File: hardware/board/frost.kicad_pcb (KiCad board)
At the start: 2 copper layers, 90 x 55 mm, 12 parts, among them U1 RK3568, U2 K4UCE3Q4AB-MGCL, U3 KLMBG2JETD-B041_C5821038, U4 RK809-5, U5 AP6256, X1 24 MHz

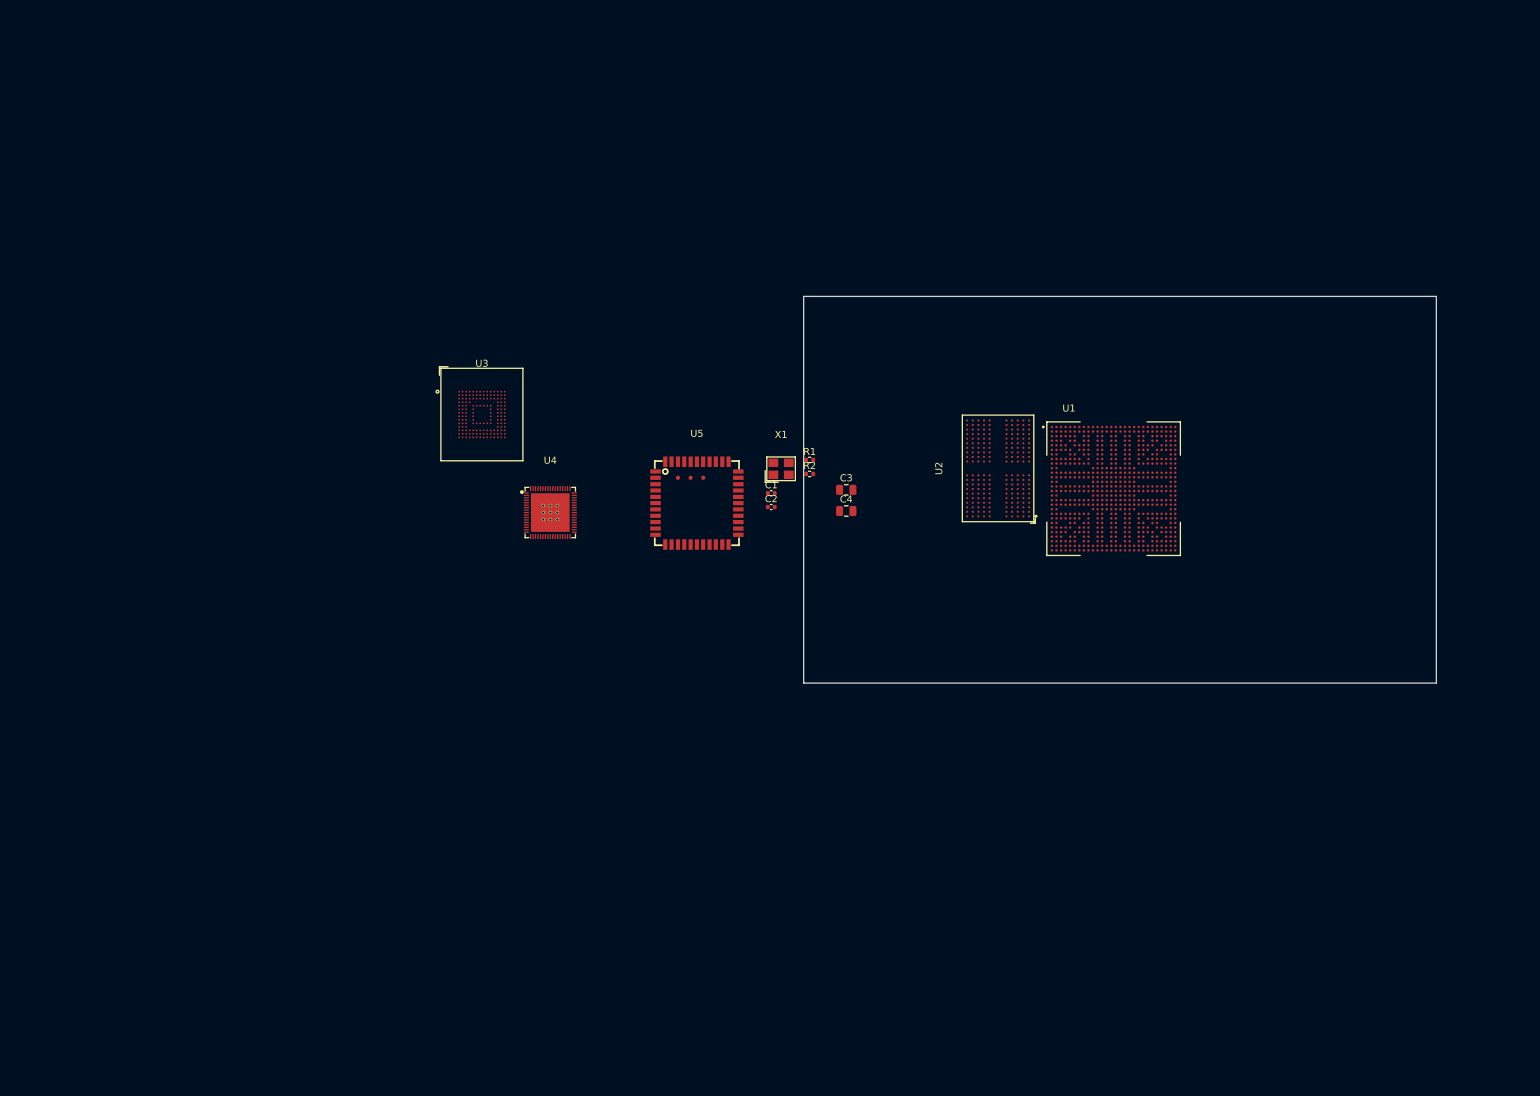
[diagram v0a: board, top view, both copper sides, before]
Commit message: MIPI IS FAKE
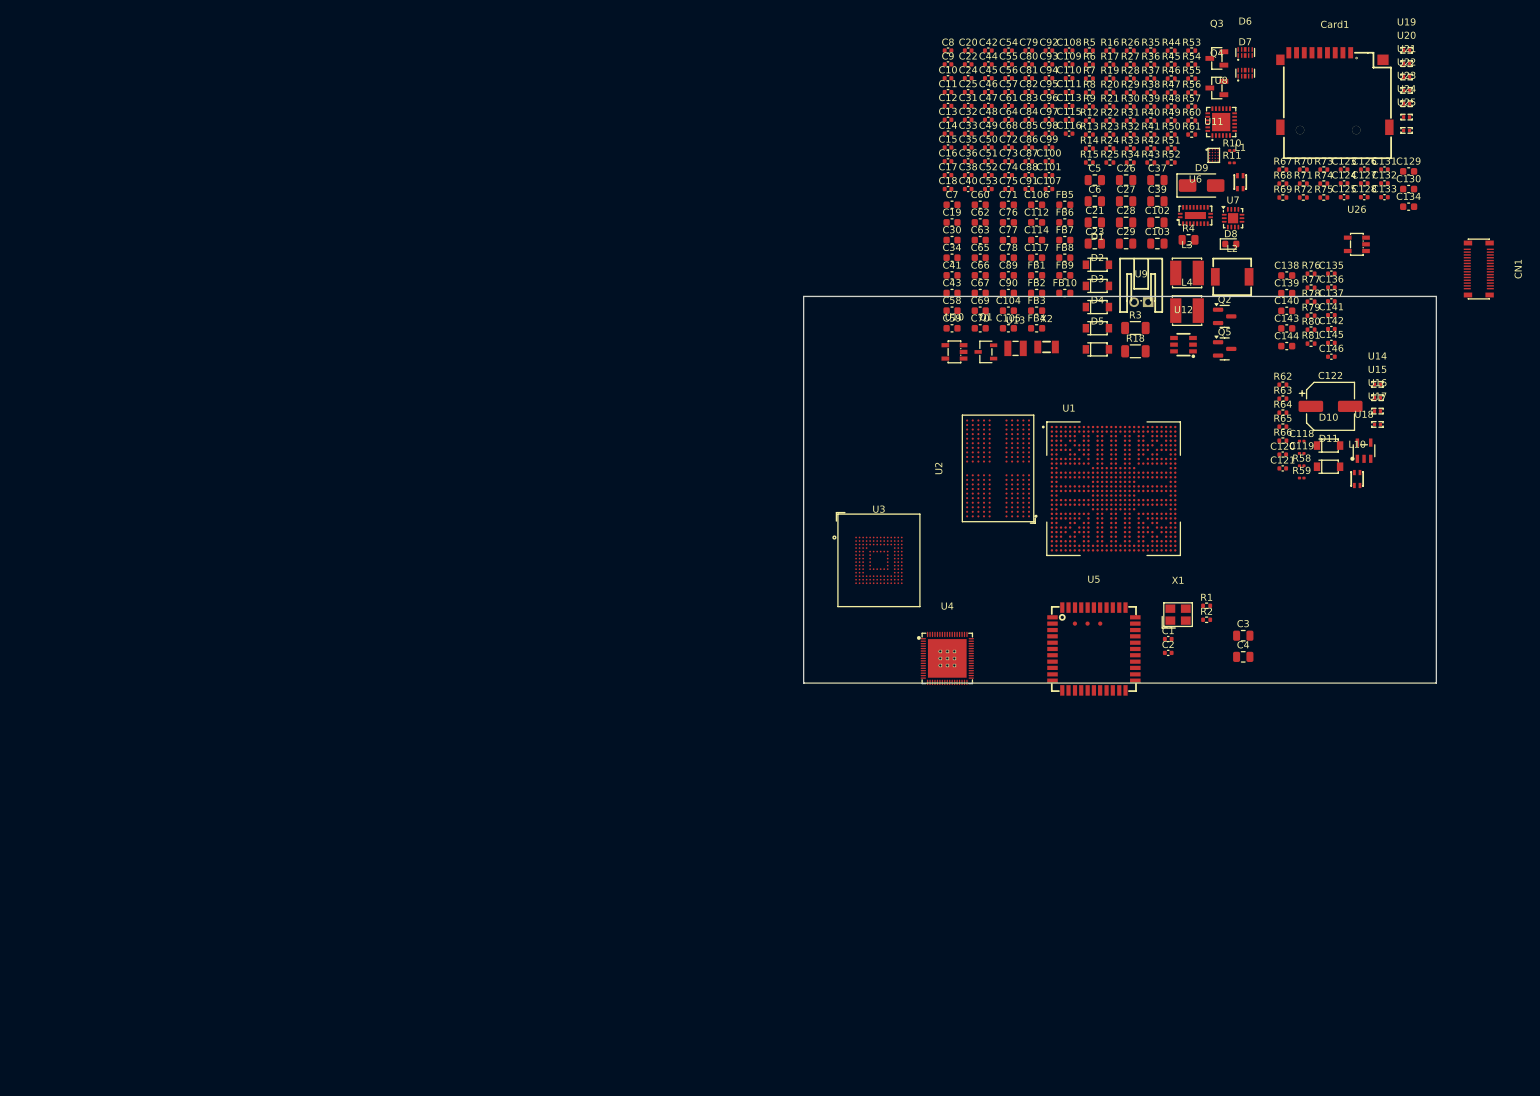
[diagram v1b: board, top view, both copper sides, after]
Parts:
- added C10: 100nF X5R 10V, Capacitor_SMD:C_0402_1005Metric, F.Cu at (149.6, 27.6)
- added C100: 680pF C0G 50V, Capacitor_SMD:C_0402_1005Metric, F.Cu at (163.9, 39.5)
- added C101: 1uF X5R 6.3V, Capacitor_SMD:C_0402_1005Metric, F.Cu at (163.9, 41.4)
- added C102: 22uF X5R 10V, Capacitor_SMD:C_0805_2012Metric, F.Cu at (179.4, 48.1)
- added C103: 22uF X5R 10V, Capacitor_SMD:C_0805_2012Metric, F.Cu at (179.4, 51.2)
- added C104: 22uF X5R 6.3V, Capacitor_SMD:C_0603_1608Metric, F.Cu at (158.2, 60.7)
- added C105: 22uF X5R 6.3V, Capacitor_SMD:C_0603_1608Metric, F.Cu at (158.2, 63.2)
- added C106: 22uF X5R 6.3V, Capacitor_SMD:C_0603_1608Metric, F.Cu at (162.2, 45.6)
- added C107: 1uF X5R 6.3V, Capacitor_SMD:C_0402_1005Metric, F.Cu at (163.9, 43.4)
- added C108: 1uF X5R 6.3V, Capacitor_SMD:C_0402_1005Metric, F.Cu at (166.8, 23.7)
- added C109: 1uF X5R 6.3V, Capacitor_SMD:C_0402_1005Metric, F.Cu at (166.8, 25.7)
- added C11: 100nF X5R 10V, Capacitor_SMD:C_0402_1005Metric, F.Cu at (149.6, 29.6)
- added C110: 1uF X5R 6.3V, Capacitor_SMD:C_0402_1005Metric, F.Cu at (166.8, 27.6)
- added C111: 1uF X5R 6.3V, Capacitor_SMD:C_0402_1005Metric, F.Cu at (166.8, 29.6)
- added C112: 10uF X5R 10V, Capacitor_SMD:C_0603_1608Metric, F.Cu at (162.2, 48.1)
- added C113: 100nF X5R 10V, Capacitor_SMD:C_0402_1005Metric, F.Cu at (166.8, 31.6)
- added C114: 10uF X5R 10V, Capacitor_SMD:C_0603_1608Metric, F.Cu at (162.2, 50.7)
- added C115: 1uF X5R 6.3V, Capacitor_SMD:C_0402_1005Metric, F.Cu at (166.8, 33.5)
- added C116: 1uF X5R 6.3V, Capacitor_SMD:C_0402_1005Metric, F.Cu at (166.8, 35.5)
- added C117: 4.7uF X5R 6.3V, Capacitor_SMD:C_0603_1608Metric, F.Cu at (162.2, 53.2)
- added C118: 100nF X5R 10V, Capacitor_SMD:C_0201_0603Metric, F.Cu at (199.9, 79.3)
- added C119: 100nF X5R 10V, Capacitor_SMD:C_0201_0603Metric, F.Cu at (199.9, 81.0)
- added C12: 100nF X5R 10V, Capacitor_SMD:C_0402_1005Metric, F.Cu at (149.6, 31.6)
- added C120: 1uF X5R 10V, Capacitor_SMD:C_0402_1005Metric, F.Cu at (197.2, 81.2)
- added C121: 100nF X5R 10V, Capacitor_SMD:C_0402_1005Metric, F.Cu at (197.2, 83.1)
- added C122: 120uF SVPF 20V, Capacitor_SMD:CP_Elec_6.3x5.9, F.Cu at (204.0, 74.3)
- added C123: 2.2uF X5R 10V, Capacitor_SMD:C_0402_1005Metric, F.Cu at (205.9, 40.6)
- added C124: 100nF X5R 10V, Capacitor_SMD:C_0402_1005Metric, F.Cu at (205.9, 42.6)
- added C125: 100nF X5R 10V, Capacitor_SMD:C_0402_1005Metric, F.Cu at (205.9, 44.6)
- added C126: 100nF X5R 10V, Capacitor_SMD:C_0402_1005Metric, F.Cu at (208.8, 40.6)
- added C127: 100nF X5R 10V, Capacitor_SMD:C_0402_1005Metric, F.Cu at (208.8, 42.6)
- added C128: 100nF X5R 10V, Capacitor_SMD:C_0402_1005Metric, F.Cu at (208.8, 44.6)
- added C129: 4.7uF X5R 6.3V, Capacitor_SMD:C_0603_1608Metric, F.Cu at (215.1, 40.9)
- added C13: 100nF X5R 10V, Capacitor_SMD:C_0402_1005Metric, F.Cu at (149.6, 33.5)
- added C130: 4.7uF X5R 6.3V, Capacitor_SMD:C_0603_1608Metric, F.Cu at (215.1, 43.4)
- added C131: 100nF X5R 10V, Capacitor_SMD:C_0402_1005Metric, F.Cu at (211.7, 40.6)
- added C132: 100nF X5R 10V, Capacitor_SMD:C_0402_1005Metric, F.Cu at (211.7, 42.6)
- added C133: 100nF X5R 10V, Capacitor_SMD:C_0402_1005Metric, F.Cu at (211.7, 44.6)
- added C134: 10uF X5R 10V, Capacitor_SMD:C_0603_1608Metric, F.Cu at (215.1, 45.9)
- added C135: 1uF X5R 6.3V, Capacitor_SMD:C_0402_1005Metric, F.Cu at (204.1, 55.4)
- added C136: 100nF X5R 10V, Capacitor_SMD:C_0402_1005Metric, F.Cu at (204.1, 57.4)
- added C137: 22pF C0G 50V, Capacitor_SMD:C_0402_1005Metric, F.Cu at (204.1, 59.4)
- added C138: 10uF X5R 10V, Capacitor_SMD:C_0603_1608Metric, F.Cu at (197.8, 55.7)
- added C139: 4.7uF X5R 6.3V, Capacitor_SMD:C_0603_1608Metric, F.Cu at (197.8, 58.2)
- added C14: 100nF X5R 10V, Capacitor_SMD:C_0402_1005Metric, F.Cu at (149.6, 35.5)
- added C140: 4.7uF X5R 6.3V, Capacitor_SMD:C_0603_1608Metric, F.Cu at (197.8, 60.7)
- added C141: 100nF X5R 10V, Capacitor_SMD:C_0402_1005Metric, F.Cu at (204.1, 61.3)
- added C142: 100nF X5R 10V, Capacitor_SMD:C_0402_1005Metric, F.Cu at (204.1, 63.3)
- added C143: 10uF X5R 10V, Capacitor_SMD:C_0603_1608Metric, F.Cu at (197.8, 63.2)
- added C144: 10uF X5R 10V, Capacitor_SMD:C_0603_1608Metric, F.Cu at (197.8, 65.7)
- added C145: 100nF X5R 10V, Capacitor_SMD:C_0402_1005Metric, F.Cu at (204.1, 65.3)
- added C146: 100nF X5R 10V, Capacitor_SMD:C_0402_1005Metric, F.Cu at (204.1, 67.2)
- added C15: 100nF X5R 10V, Capacitor_SMD:C_0402_1005Metric, F.Cu at (149.6, 37.5)
- added C16: 220pF C0G 25V, Capacitor_SMD:C_0402_1005Metric, F.Cu at (149.6, 39.5)
- added C17: 220pF C0G 25V, Capacitor_SMD:C_0402_1005Metric, F.Cu at (149.6, 41.4)
- added C18: 1uF X5R 10V, Capacitor_SMD:C_0402_1005Metric, F.Cu at (149.6, 43.4)
- added C19: 10uF X5R 10V, Capacitor_SMD:C_0603_1608Metric, F.Cu at (150.2, 48.1)
- added C20: 100nF X5R 10V, Capacitor_SMD:C_0402_1005Metric, F.Cu at (152.5, 23.7)
- added C21: 10uF X5R 25V, Capacitor_SMD:C_0805_2012Metric, F.Cu at (170.5, 48.1)
- added C22: 100pF C0G 50V, Capacitor_SMD:C_0402_1005Metric, F.Cu at (152.5, 25.7)
- added C23: 10uF X5R 25V, Capacitor_SMD:C_0805_2012Metric, F.Cu at (170.5, 51.2)
- added C24: 4.7uF X5R 10V, Capacitor_SMD:C_0402_1005Metric, F.Cu at (152.5, 27.6)
- added C25: 47nF X5R 25V, Capacitor_SMD:C_0402_1005Metric, F.Cu at (152.5, 29.6)
- added C26: 10uF X5R 10V, Capacitor_SMD:C_0805_2012Metric, F.Cu at (174.9, 42.1)
- added C27: 10uF X5R 10V, Capacitor_SMD:C_0805_2012Metric, F.Cu at (174.9, 45.1)
- added C28: 10uF X5R 10V, Capacitor_SMD:C_0805_2012Metric, F.Cu at (174.9, 48.1)
- added C29: 10uF X5R 10V, Capacitor_SMD:C_0805_2012Metric, F.Cu at (174.9, 51.2)
- added C30: 10uF X5R 10V, Capacitor_SMD:C_0603_1608Metric, F.Cu at (150.2, 50.7)
- added C31: 100nF X5R 10V, Capacitor_SMD:C_0402_1005Metric, F.Cu at (152.5, 31.6)
- added C32: 100nF X5R 10V, Capacitor_SMD:C_0402_1005Metric, F.Cu at (152.5, 33.5)
- added C33: 22pF C0G 50V, Capacitor_SMD:C_0402_1005Metric, F.Cu at (152.5, 35.5)
- added C34: 22uF X5R 6.3V, Capacitor_SMD:C_0603_1608Metric, F.Cu at (150.2, 53.2)
- added C35: 100nF X5R 10V, Capacitor_SMD:C_0402_1005Metric, F.Cu at (152.5, 37.5)
- added C36: 100nF X5R 16V, Capacitor_SMD:C_0402_1005Metric, F.Cu at (152.5, 39.5)
- added C37: 10uF X5R 10V, Capacitor_SMD:C_0805_2012Metric, F.Cu at (179.4, 42.1)
- added C38: 22pF C0G 50V, Capacitor_SMD:C_0402_1005Metric, F.Cu at (152.5, 41.4)
- added C39: 22uF X5R 10V, Capacitor_SMD:C_0805_2012Metric, F.Cu at (179.4, 45.1)
- added C40: 100nF X5R 10V, Capacitor_SMD:C_0402_1005Metric, F.Cu at (152.5, 43.4)
- added C41: 10uF X5R 10V, Capacitor_SMD:C_0603_1608Metric, F.Cu at (150.2, 55.7)
- added C42: 100nF X5R 10V, Capacitor_SMD:C_0402_1005Metric, F.Cu at (155.3, 23.7)
- added C43: 10uF X5R 10V, Capacitor_SMD:C_0603_1608Metric, F.Cu at (150.2, 58.2)
- added C44: 4.7uF X5R 6.3V, Capacitor_SMD:C_0402_1005Metric, F.Cu at (155.3, 25.7)
- added C45: 1uF X5R 6.3V, Capacitor_SMD:C_0402_1005Metric, F.Cu at (155.3, 27.6)
- added C46: 1uF X5R 6.3V, Capacitor_SMD:C_0402_1005Metric, F.Cu at (155.3, 29.6)
- added C47: 1uF X5R 6.3V, Capacitor_SMD:C_0402_1005Metric, F.Cu at (155.3, 31.6)
- added C48: 1uF X5R 6.3V, Capacitor_SMD:C_0402_1005Metric, F.Cu at (155.3, 33.5)
- added C49: 1uF X5R 6.3V, Capacitor_SMD:C_0402_1005Metric, F.Cu at (155.3, 35.5)
- added C5: 10uF X5R 25V, Capacitor_SMD:C_0805_2012Metric, F.Cu at (170.5, 42.1)
- added C50: 1uF X5R 10V, Capacitor_SMD:C_0402_1005Metric, F.Cu at (155.3, 37.5)
- added C51: 20pF C0G 50V, Capacitor_SMD:C_0402_1005Metric, F.Cu at (155.3, 39.5)
- added C52: 20pF C0G 50V, Capacitor_SMD:C_0402_1005Metric, F.Cu at (155.3, 41.4)
- added C53: 100nF X5R 10V, Capacitor_SMD:C_0402_1005Metric, F.Cu at (155.3, 43.4)
- added C54: 100nF X5R 10V, Capacitor_SMD:C_0402_1005Metric, F.Cu at (158.2, 23.7)
- added C55: 100nF X5R 16V, Capacitor_SMD:C_0402_1005Metric, F.Cu at (158.2, 25.7)
- added C56: 100nF X5R 16V, Capacitor_SMD:C_0402_1005Metric, F.Cu at (158.2, 27.6)
- added C57: 1uF X5R 10V, Capacitor_SMD:C_0402_1005Metric, F.Cu at (158.2, 29.6)
- added C58: 22uF X5R 6.3V, Capacitor_SMD:C_0603_1608Metric, F.Cu at (150.2, 60.7)
- added C59: 22uF X5R 6.3V, Capacitor_SMD:C_0603_1608Metric, F.Cu at (150.2, 63.2)
- added C6: 10uF X5R 25V, Capacitor_SMD:C_0805_2012Metric, F.Cu at (170.5, 45.1)
- added C60: 22uF X5R 6.3V, Capacitor_SMD:C_0603_1608Metric, F.Cu at (154.2, 45.6)
- added C61: 100nF X5R 10V, Capacitor_SMD:C_0402_1005Metric, F.Cu at (158.2, 31.6)
- added C62: 22uF X5R 6.3V, Capacitor_SMD:C_0603_1608Metric, F.Cu at (154.2, 48.1)
- added C63: 22uF X5R 6.3V, Capacitor_SMD:C_0603_1608Metric, F.Cu at (154.2, 50.7)
- added C64: 100nF X5R 10V, Capacitor_SMD:C_0402_1005Metric, F.Cu at (158.2, 33.5)
- added C65: 10uF X5R 10V, Capacitor_SMD:C_0603_1608Metric, F.Cu at (154.2, 53.2)
- added C66: 22uF X5R 6.3V, Capacitor_SMD:C_0603_1608Metric, F.Cu at (154.2, 55.7)
- added C67: 22uF X5R 6.3V, Capacitor_SMD:C_0603_1608Metric, F.Cu at (154.2, 58.2)
- added C68: 100nF X5R 10V, Capacitor_SMD:C_0402_1005Metric, F.Cu at (158.2, 35.5)
- added C69: 10uF X5R 10V, Capacitor_SMD:C_0603_1608Metric, F.Cu at (154.2, 60.7)
- added C7: 10uF X5R 10V, Capacitor_SMD:C_0603_1608Metric, F.Cu at (150.2, 45.6)
- added C70: 22uF X5R 6.3V, Capacitor_SMD:C_0603_1608Metric, F.Cu at (154.2, 63.2)
- added C71: 10uF X5R 10V, Capacitor_SMD:C_0603_1608Metric, F.Cu at (158.2, 45.6)
- added C72: 1uF X5R 6.3V, Capacitor_SMD:C_0402_1005Metric, F.Cu at (158.2, 37.5)
- added C73: 1uF X5R 6.3V, Capacitor_SMD:C_0402_1005Metric, F.Cu at (158.2, 39.5)
- added C74: 1uF X5R 10V, Capacitor_SMD:C_0402_1005Metric, F.Cu at (158.2, 41.4)
- added C75: 1uF X5R 6.3V, Capacitor_SMD:C_0402_1005Metric, F.Cu at (158.2, 43.4)
- added C76: 10uF X5R 10V, Capacitor_SMD:C_0603_1608Metric, F.Cu at (158.2, 48.1)
- added C77: 22uF X5R 6.3V, Capacitor_SMD:C_0603_1608Metric, F.Cu at (158.2, 50.7)
- added C78: 22uF X5R 6.3V, Capacitor_SMD:C_0603_1608Metric, F.Cu at (158.2, 53.2)
- added C79: 1uF X5R 6.3V, Capacitor_SMD:C_0402_1005Metric, F.Cu at (161.1, 23.7)
- added C8: 100nF X5R 10V, Capacitor_SMD:C_0402_1005Metric, F.Cu at (149.6, 23.7)
- added C80: 100nF X5R 10V, Capacitor_SMD:C_0402_1005Metric, F.Cu at (161.1, 25.7)
- added C81: 1uF X5R 6.3V, Capacitor_SMD:C_0402_1005Metric, F.Cu at (161.1, 27.6)
- added C82: 1uF X5R 6.3V, Capacitor_SMD:C_0402_1005Metric, F.Cu at (161.1, 29.6)
- added C83: 1uF X5R 10V, Capacitor_SMD:C_0402_1005Metric, F.Cu at (161.1, 31.6)
- added C84: 1uF X5R 10V, Capacitor_SMD:C_0402_1005Metric, F.Cu at (161.1, 33.5)
- added C85: 1uF X5R 10V, Capacitor_SMD:C_0402_1005Metric, F.Cu at (161.1, 35.5)
- added C86: 4.7uF X5R 6.3V, Capacitor_SMD:C_0402_1005Metric, F.Cu at (161.1, 37.5)
- added C87: 1uF X5R 6.3V, Capacitor_SMD:C_0402_1005Metric, F.Cu at (161.1, 39.5)
- added C88: 1uF X5R 6.3V, Capacitor_SMD:C_0402_1005Metric, F.Cu at (161.1, 41.4)
- added C89: 10uF X5R 10V, Capacitor_SMD:C_0603_1608Metric, F.Cu at (158.2, 55.7)
- added C9: 100nF X5R 10V, Capacitor_SMD:C_0402_1005Metric, F.Cu at (149.6, 25.7)
- added C90: 4.7uF X5R 10V, Capacitor_SMD:C_0603_1608Metric, F.Cu at (158.2, 58.2)
- added C91: 1uF X5R 6.3V, Capacitor_SMD:C_0402_1005Metric, F.Cu at (161.1, 43.4)
- added C92: 2.2uF X5R 10V, Capacitor_SMD:C_0402_1005Metric, F.Cu at (163.9, 23.7)
- added C93: 1uF X5R 6.3V, Capacitor_SMD:C_0402_1005Metric, F.Cu at (163.9, 25.7)
- added C94: 1uF X5R 6.3V, Capacitor_SMD:C_0402_1005Metric, F.Cu at (163.9, 27.6)
- added C95: 27pF C0G 50V, Capacitor_SMD:C_0402_1005Metric, F.Cu at (163.9, 29.6)
- added C96: 27pF C0G 50V, Capacitor_SMD:C_0402_1005Metric, F.Cu at (163.9, 31.6)
- added C97: 100nF X5R 10V, Capacitor_SMD:C_0402_1005Metric, F.Cu at (163.9, 33.5)
- added C98: 100nF X5R 10V, Capacitor_SMD:C_0402_1005Metric, F.Cu at (163.9, 35.5)
- added C99: 680pF C0G 50V, Capacitor_SMD:C_0402_1005Metric, F.Cu at (163.9, 37.5)
- added CN1: AXT530124_C2924271, lcsc:CONN-SMD_30P-P0.40_AXT530124, F.Cu at (225.1, 54.8)
- added Card1: TF PUSH, lcsc:TF-SMD_TF-PUSH, F.Cu at (204.6, 29.3)
- added D1: BZT52C5V1_C173407, lcsc:SOD-123_L2.7-W1.6-LS3.7-RD, F.Cu at (170.8, 54.2)
- added D10: BZT52C5V1_C173407, lcsc:SOD-123_L2.7-W1.6-LS3.7-RD, F.Cu at (203.7, 79.9)
- added D11: BZT52C5V1_C173407, lcsc:SOD-123_L2.7-W1.6-LS3.7-RD, F.Cu at (203.7, 82.9)
- added D2: BZT52C5V1_C173407, lcsc:SOD-123_L2.7-W1.6-LS3.7-RD, F.Cu at (170.8, 57.2)
- added D3: BZT52C5V1_C173407, lcsc:SOD-123_L2.7-W1.6-LS3.7-RD, F.Cu at (170.8, 60.2)
- added D4: BZT52C5V1_C173407, lcsc:SOD-123_L2.7-W1.6-LS3.7-RD, F.Cu at (170.8, 63.2)
- added D5: BZT52C5V1_C173407, lcsc:SOD-123_L2.7-W1.6-LS3.7-RD, F.Cu at (170.8, 66.2)
- added D6: ESD5344D, lcsc:DFN2510-10_L2.5-W1.0-P0.50-BL, F.Cu at (191.9, 24.0)
- added D7: ESD5344D, lcsc:DFN2510-10_L2.5-W1.0-P0.50-BL, F.Cu at (191.9, 26.9)
- added D8: LED, LED_SMD:LED_0603_1608Metric, F.Cu at (189.8, 51.2)
- added D9: SS32, Diode_SMD:D_SMA, F.Cu at (185.7, 42.9)
- added FB1: 120@100MHz 0.03R, Inductor_SMD:L_0603_1608Metric, F.Cu at (162.2, 55.7)
- added FB10: 120@100MHz 0.03R, Inductor_SMD:L_0603_1608Metric, F.Cu at (166.2, 58.2)
- added FB2: 120@100MHz 0.03R, Inductor_SMD:L_0603_1608Metric, F.Cu at (162.2, 58.2)
- added FB3: 120@100MHz 0.03R, Inductor_SMD:L_0603_1608Metric, F.Cu at (162.2, 60.7)
- added FB4: 120@100MHz 0.03R, Inductor_SMD:L_0603_1608Metric, F.Cu at (162.2, 63.2)
- added FB5: 180@100M 1.5A, Inductor_SMD:L_0603_1608Metric, F.Cu at (166.2, 45.6)
- added FB6: 180@100M 1.5A, Inductor_SMD:L_0603_1608Metric, F.Cu at (166.2, 48.1)
- added FB7: 120@100MHz 0.03R, Inductor_SMD:L_0603_1608Metric, F.Cu at (166.2, 50.7)
- added FB8: 120@100MHz 0.03R, Inductor_SMD:L_0603_1608Metric, F.Cu at (166.2, 53.2)
- added FB9: 120@100MHz 0.03R, Inductor_SMD:L_0603_1608Metric, F.Cu at (166.2, 55.7)
- added L1: L_Iron_Coupled_Small, lcsc:FILTER-SMD_4P-L2.0-W1.2-BL_DLW21H, F.Cu at (191.2, 42.4)
- added L10: L_Iron_Coupled_Small, lcsc:FILTER-SMD_4P-L2.0-W1.2-BL_DLW21H, F.Cu at (207.8, 84.7)
- added L2: SLO0520H1R0MTT, lcsc:IND-SMD_L5.4-W5.1, F.Cu at (190.0, 55.9)
- added L3: LVF404026-2R2M-N, lcsc:IND-SMD_L4.0-W4.0, F.Cu at (183.6, 55.3)
- added L4: LVF404026-2R2M-N, lcsc:IND-SMD_L4.0-W4.0, F.Cu at (183.6, 60.7)
- added Q1: WPM3407-3/TR, lcsc:SOT-23-3_L3.0-W1.7-P0.95-LS2.9-BR, F.Cu at (155.0, 66.6)
- added Q2: SS8050, Package_TO_SOT_SMD:SOT-23, F.Cu at (188.9, 61.5)
- added Q3: WPM2015-3/TR_C7472861, lcsc:SOT-23-3_L2.9-W1.3-P1.90-LS2.4-BR, F.Cu at (187.8, 24.8)
- added Q4: WPM2015-3/TR_C7472861, lcsc:SOT-23-3_L2.9-W1.3-P1.90-LS2.4-BR, F.Cu at (187.8, 29.0)
- added Q5: SS8050, Package_TO_SOT_SMD:SOT-23, F.Cu at (188.9, 66.1)
- added R10: 0R 5%, Resistor_SMD:R_0201_0603Metric, F.Cu at (190.0, 37.9)
- added R11: 0R 5%, Resistor_SMD:R_0201_0603Metric, F.Cu at (190.0, 39.7)
- added R12: 0R 5%, Resistor_SMD:R_0402_1005Metric, F.Cu at (169.7, 33.7)
- added R13: 330R 5%, Resistor_SMD:R_0402_1005Metric, F.Cu at (169.7, 35.6)
- added R14: 100R 5%, Resistor_SMD:R_0402_1005Metric, F.Cu at (169.7, 37.6)
- added R15: 5.1K 1%, Resistor_SMD:R_0402_1005Metric, F.Cu at (169.7, 39.6)
- added R16: 30K 1%, Resistor_SMD:R_0402_1005Metric, F.Cu at (172.6, 23.7)
- added R17: 10K 5%, Resistor_SMD:R_0402_1005Metric, F.Cu at (172.6, 25.7)
- added R18: 0.01R 1%, Resistor_SMD:R_1206_3216Metric, F.Cu at (176.2, 66.5)
- added R19: 0R 5%, Resistor_SMD:R_0402_1005Metric, F.Cu at (172.6, 27.7)
- added R20: 10K 5%, Resistor_SMD:R_0402_1005Metric, F.Cu at (172.6, 29.7)
- added R21: 232K 1%, Resistor_SMD:R_0402_1005Metric, F.Cu at (172.6, 31.7)
- added R22: 49.9K 1%, Resistor_SMD:R_0402_1005Metric, F.Cu at (172.6, 33.7)
- added R23: 100K 5%, Resistor_SMD:R_0402_1005Metric, F.Cu at (172.6, 35.6)
- added R24: 10K 5%, Resistor_SMD:R_0402_1005Metric, F.Cu at (172.6, 37.6)
- added R25: 51K 5%, Resistor_SMD:R_0402_1005Metric, F.Cu at (172.6, 39.6)
- added R26: 10K 5%, Resistor_SMD:R_0402_1005Metric, F.Cu at (175.5, 23.7)
- added R27: 360K 1%, Resistor_SMD:R_0402_1005Metric, F.Cu at (175.5, 25.7)
- added R28: 47K 1%, Resistor_SMD:R_0402_1005Metric, F.Cu at (175.5, 27.7)
- added R29: 10K 5%, Resistor_SMD:R_0402_1005Metric, F.Cu at (175.5, 29.7)
- added R3: 0R, Resistor_SMD:R_1206_3216Metric, F.Cu at (176.2, 63.2)
- added R30: 100K 5%, Resistor_SMD:R_0402_1005Metric, F.Cu at (175.5, 31.7)
- added R31: 0R 5%, Resistor_SMD:R_0402_1005Metric, F.Cu at (175.5, 33.7)
- added R32: 0R 5%, Resistor_SMD:R_0402_1005Metric, F.Cu at (175.5, 35.6)
- added R33: 0R 5%, Resistor_SMD:R_0402_1005Metric, F.Cu at (175.5, 37.6)
- added R34: 10K 5%, Resistor_SMD:R_0402_1005Metric, F.Cu at (175.5, 39.6)
- added R35: 22R 5%, Resistor_SMD:R_0402_1005Metric, F.Cu at (178.4, 23.7)
- added R36: 22R 5%, Resistor_SMD:R_0402_1005Metric, F.Cu at (178.4, 25.7)
- added R37: 30K 1%, Resistor_SMD:R_0402_1005Metric, F.Cu at (178.4, 27.7)
- added R38: 20K 1%, Resistor_SMD:R_0402_1005Metric, F.Cu at (178.4, 29.7)
- added R39: 30K 1%, Resistor_SMD:R_0402_1005Metric, F.Cu at (178.4, 31.7)
- added R4: 470R 5%, Resistor_SMD:R_0805_2012Metric, F.Cu at (183.8, 50.6)
- added R40: 100R 5%, Resistor_SMD:R_0402_1005Metric, F.Cu at (178.4, 33.7)
- added R41: 100R 5%, Resistor_SMD:R_0402_1005Metric, F.Cu at (178.4, 35.6)
- added R42: 100R 5%, Resistor_SMD:R_0402_1005Metric, F.Cu at (178.4, 37.6)
- added R43: 47K 1%, Resistor_SMD:R_0402_1005Metric, F.Cu at (178.4, 39.6)
- added R44: 120K 1%, Resistor_SMD:R_0402_1005Metric, F.Cu at (181.3, 23.7)
- added R45: 0R 5%, Resistor_SMD:R_0402_1005Metric, F.Cu at (181.3, 25.7)
- added R46: 30K 5%, Resistor_SMD:R_0402_1005Metric, F.Cu at (181.3, 27.7)
- added R47: 100K 5%, Resistor_SMD:R_0402_1005Metric, F.Cu at (181.3, 29.7)
- added R48: 51K 5%, Resistor_SMD:R_0402_1005Metric, F.Cu at (181.3, 31.7)
- added R49: 100R 5%, Resistor_SMD:R_0402_1005Metric, F.Cu at (181.3, 33.7)
- added R5: 10K 5%, Resistor_SMD:R_0402_1005Metric, F.Cu at (169.7, 23.7)
- added R50: 100K 5%, Resistor_SMD:R_0402_1005Metric, F.Cu at (181.3, 35.6)
- added R51: 10K 5%, Resistor_SMD:R_0402_1005Metric, F.Cu at (181.3, 37.6)
- added R52: 51K 5%, Resistor_SMD:R_0402_1005Metric, F.Cu at (181.3, 39.6)
- added R53: 10K 5%, Resistor_SMD:R_0402_1005Metric, F.Cu at (184.3, 23.7)
- added R54: 0R 5%, Resistor_SMD:R_0402_1005Metric, F.Cu at (184.3, 25.7)
- added R55: 0R 5%, Resistor_SMD:R_0402_1005Metric, F.Cu at (184.3, 27.7)
- added R56: 0R 5%, Resistor_SMD:R_0402_1005Metric, F.Cu at (184.3, 29.7)
- added R57: 10K 5%, Resistor_SMD:R_0402_1005Metric, F.Cu at (184.3, 31.7)
- added R58: 0R 5%, Resistor_SMD:R_0201_0603Metric, F.Cu at (199.9, 82.8)
- added R59: 0R 5%, Resistor_SMD:R_0201_0603Metric, F.Cu at (199.9, 84.5)
- added R6: 15K 5%, Resistor_SMD:R_0402_1005Metric, F.Cu at (169.7, 25.7)
- added R60: 0R 5%, Resistor_SMD:R_0402_1005Metric, F.Cu at (184.3, 33.7)
- added R61: 0R 5%, Resistor_SMD:R_0402_1005Metric, F.Cu at (184.3, 35.6)
- added R62: 0R 5%, Resistor_SMD:R_0402_1005Metric, F.Cu at (197.2, 71.2)
- added R63: 0R 5%, Resistor_SMD:R_0402_1005Metric, F.Cu at (197.2, 73.2)
- added R64: 2.2R 5%, Resistor_SMD:R_0402_1005Metric, F.Cu at (197.2, 75.2)
- added R65: 2.2R 5%, Resistor_SMD:R_0402_1005Metric, F.Cu at (197.2, 77.2)
- added R66: 4.7K 5%, Resistor_SMD:R_0402_1005Metric, F.Cu at (197.2, 79.2)
- added R67: 10K 5%, Resistor_SMD:R_0402_1005Metric, F.Cu at (197.2, 40.6)
- added R68: 10K 5%, Resistor_SMD:R_0402_1005Metric, F.Cu at (197.2, 42.6)
- added R69: 10K 5%, Resistor_SMD:R_0402_1005Metric, F.Cu at (197.2, 44.6)
- added R7: 2.2R 5%, Resistor_SMD:R_0402_1005Metric, F.Cu at (169.7, 27.7)
- added R70: 22R 5%, Resistor_SMD:R_0402_1005Metric, F.Cu at (200.1, 40.6)
- added R71: 22R 5%, Resistor_SMD:R_0402_1005Metric, F.Cu at (200.1, 42.6)
- added R72: 22R 5%, Resistor_SMD:R_0402_1005Metric, F.Cu at (200.1, 44.6)
- added R73: 22R 5%, Resistor_SMD:R_0402_1005Metric, F.Cu at (203.1, 40.6)
- added R74: 22R 5%, Resistor_SMD:R_0402_1005Metric, F.Cu at (203.1, 42.6)
- added R75: 22R 5%, Resistor_SMD:R_0402_1005Metric, F.Cu at (203.1, 44.6)
- added R76: 10K 5%, Resistor_SMD:R_0402_1005Metric, F.Cu at (201.2, 55.4)
- added R77: 200K 1%, Resistor_SMD:R_0402_1005Metric, F.Cu at (201.2, 57.4)
- added R78: 390K 1%, Resistor_SMD:R_0402_1005Metric, F.Cu at (201.2, 59.4)
- added R79: 0R 5%, Resistor_SMD:R_0402_1005Metric, F.Cu at (201.2, 61.4)
- added R8: 2.2R 5%, Resistor_SMD:R_0402_1005Metric, F.Cu at (169.7, 29.7)
- added R80: 0R 5%, Resistor_SMD:R_0402_1005Metric, F.Cu at (201.2, 63.4)
- added R81: 0R 5%, Resistor_SMD:R_0402_1005Metric, F.Cu at (201.2, 65.4)
- added R9: 0R 5%, Resistor_SMD:R_0402_1005Metric, F.Cu at (169.7, 31.7)
- added U10: SY8088AAC, lcsc:SOT-23-5_L3.0-W1.7-P0.95-LS2.8-BR, F.Cu at (150.5, 66.6)
- added U11: RK860-0, lcsc:WLCSP-20_L2.0-W1.6-R5-C4-P0.40-TL, F.Cu at (187.4, 38.6)
- added U12: SY7208ABC, lcsc:SOT-23-6_L2.9-W1.6-P0.95-LS2.8-BR, F.Cu at (183.1, 65.5)
- added U13: FTC252012SR24MBCA, lcsc:IND-SMD_L2.5-W2.0_MHCHL2520, F.Cu at (159.2, 66.1)
- added U14: ESD5311X, lcsc:DFN1006-2L-BI, F.Cu at (210.7, 71.2)
- added U15: ESD5311X, lcsc:DFN1006-2L-BI, F.Cu at (210.7, 73.1)
- added U16: ESD5311X, lcsc:DFN1006-2L-BI, F.Cu at (210.7, 75.0)
- added U17: ESD5311X, lcsc:DFN1006-2L-BI, F.Cu at (210.7, 76.9)
- added U18: SY6280AAC, lcsc:SOT-23-5_L3.0-W1.7-P0.95-LS2.8-BL, F.Cu at (208.8, 80.6)
- added U19: ESD5311X, lcsc:DFN1006-2L-BI, F.Cu at (214.8, 23.7)
- added U20: ESD5311X, lcsc:DFN1006-2L-BI, F.Cu at (214.8, 25.6)
- added U21: ESD5311X, lcsc:DFN1006-2L-BI, F.Cu at (214.8, 27.5)
- added U22: ESD5311X, lcsc:DFN1006-2L-BI, F.Cu at (214.8, 29.4)
- added U23: ESD5311X, lcsc:DFN1006-2L-BI, F.Cu at (214.8, 31.3)
- added U24: ESD5311X, lcsc:DFN1006-2L-BI, F.Cu at (214.8, 33.2)
- added U25: ESD5311X, lcsc:DFN1006-2L-BI, F.Cu at (214.8, 35.1)
- added U26: LP3983SAB5F-08, lcsc:SOT-23-5_L3.0-W1.7-P0.95-LS2.8-BR, F.Cu at (207.8, 51.3)
- added U6: TMUXHS4212RKSR, lcsc:TQFN-20_L4.5-W2.5-P0.50-BL-EP3.0, F.Cu at (184.8, 47.2)
- added U7: FUSB302BMPX, Package_DFN_QFN:WQFN-14-1EP_2.5x2.5mm_P0.5mm_EP1.45x1.45mm, F.Cu at (190.2, 47.5)
- added U8: BQ25890RTWR, lcsc:WQFN-24_L4.0-W4.0-P0.50-BL-EP, F.Cu at (188.5, 33.9)
- added U9: S2B-PH-K-S(LF)(SN), lcsc:CONN-TH_S2B-PH-K-S-LF-SN, F.Cu at (177.1, 59.5)
- added X2: Q13FC1350000400, lcsc:FC-135R_L3.2-W1.5, F.Cu at (163.6, 65.9)
- moved U3 60.2 mm to (139.8, 96.2)
- moved C1 60.2 mm to (180.9, 107.4)
- moved C2 60.2 mm to (180.9, 109.4)
- moved C3 60.2 mm to (191.6, 106.9)
- moved R1 60.2 mm to (186.4, 102.7)
- moved R2 60.2 mm to (186.4, 104.7)
- moved U4 60.2 mm to (149.5, 110.2)
- moved U5 60.2 mm to (170.3, 108.8)
- moved C4 60.2 mm to (191.6, 109.9)
- moved X1 60.2 mm to (182.3, 103.9)
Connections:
- C3 pad 1: unconnected-(C3-Pad1) -> VBUS_TYPEC_0
- C3 pad 2: unconnected-(C3-Pad2) -> GND
- C4 pad 1: unconnected-(C4-Pad1) -> VBUS_TYPEC_0
- C4 pad 2: unconnected-(C4-Pad2) -> GND
- U3 pad A3: unconnected-(U3-DAT0-PadA3) -> eMMC_D0
- U3 pad A4: unconnected-(U3-DAT1-PadA4) -> eMMC_D1
- U3 pad A5: unconnected-(U3-DAT2-PadA5) -> eMMC_D2
- U3 pad A6: unconnected-(U3-VSS-PadA6) -> GND
- U3 pad B2: unconnected-(U3-DAT3-PadB2) -> eMMC_D3
- U3 pad B3: unconnected-(U3-DAT4-PadB3) -> eMMC_D4
- U3 pad B4: unconnected-(U3-DAT5-PadB4) -> eMMC_D5
- U3 pad B5: unconnected-(U3-DAT6-PadB5) -> eMMC_D6
- U3 pad B6: unconnected-(U3-DAT7-PadB6) -> eMMC_D7
- U3 pad C2: unconnected-(U3-VDDI-PadC2) -> Net-(U3-VDDI)
- U3 pad C4: unconnected-(U3-VSS-PadC4) -> GND
- U3 pad C6: unconnected-(U3-VDD-PadC6) -> VCCIO_FLASH
- U3 pad E6: unconnected-(U3-VDDF-PadE6) -> VCC_3V3
- U3 pad E7: unconnected-(U3-VSS-PadE7) -> GND
- U3 pad F5: unconnected-(U3-VDDF-PadF5) -> VCC_3V3
- U3 pad G5: unconnected-(U3-VSS-PadG5) -> GND
- U3 pad H10: unconnected-(U3-VSS-PadH10) -> GND
- U3 pad H5: unconnected-(U3-DATASTROBE-PadH5) -> eMMC_DATA_STROBE
- U3 pad J10: unconnected-(U3-VDDF-PadJ10) -> VCC_3V3
- U3 pad J5: unconnected-(U3-VSS-PadJ5) -> GND
- U3 pad K5: unconnected-(U3-RSTN-PadK5) -> eMMC_RSTn
- U3 pad K8: unconnected-(U3-VSS-PadK8) -> GND
- U3 pad K9: unconnected-(U3-VDDF-PadK9) -> VCC_3V3
- U3 pad M4: unconnected-(U3-VDD-PadM4) -> VCCIO_FLASH
- U3 pad M5: unconnected-(U3-CDM-PadM5) -> eMMC_CMD
- U3 pad M6: unconnected-(U3-CLK-PadM6) -> eMMC_CLKOUT
- U3 pad N2: unconnected-(U3-VSS-PadN2) -> GND
- U3 pad N4: unconnected-(U3-VDD-PadN4) -> VCCIO_FLASH
- U3 pad N5: unconnected-(U3-VSS-PadN5) -> GND
- U3 pad P3: unconnected-(U3-VDD-PadP3) -> VCCIO_FLASH
- U3 pad P4: unconnected-(U3-VSS-PadP4) -> GND
- U3 pad P5: unconnected-(U3-VDD-PadP5) -> VCCIO_FLASH
- U3 pad P6: unconnected-(U3-VSS-PadP6) -> GND
- U4 pad 1: unconnected-(U4-SCL-Pad1) -> Net-(U4-SCL)
- U4 pad 10: unconnected-(U4-VCC2-Pad10) -> VCC_SYSIN
- U4 pad 11: unconnected-(U4-VCC1-Pad11) -> VCC_SYSIN
- U4 pad 12: unconnected-(U4-SW1-Pad12) -> Net-(U4-SW1)
- U4 pad 13: unconnected-(U4-FB1-Pad13) -> VDD_LOGIC
- U4 pad 14: unconnected-(U4-LRCLK-Pad14) -> I2S1_LRCK_TX_M0_PMIC
- U4 pad 15: unconnected-(U4-BCLK-Pad15) -> I2S1_SCLK_TX_M0_PMIC
- U4 pad 16: unconnected-(U4-MCLK-Pad16) -> I2S1_MCLK_M0_PMIC
- U4 pad 17: unconnected-(U4-SDI-Pad17) -> I2S1_SDO0_M0_PMIC
- U4 pad 18: unconnected-(U4-SDO/PDMDATA-Pad18) -> I2S1_SDI0_M0/PDM_SDI0_M0_PMIC
- U4 pad 19: unconnected-(U4-PDMCLK-Pad19) -> PDM_CLK0_M0_PMIC
- U4 pad 2: unconnected-(U4-SDA-Pad2) -> Net-(U4-SDA)
- U4 pad 20: unconnected-(U4-LDO3-Pad20) -> VDDA0V9_PMU
- U4 pad 21: unconnected-(U4-LDO2-Pad21) -> VDDA_0V9_P
- U4 pad 22: unconnected-(U4-VCC5-Pad22) -> VCC_SYSIN
- U4 pad 23: unconnected-(U4-LDO1-Pad23) -> VDDA0V9_IMAGE_P
- U4 pad 24: unconnected-(U4-VCC3-Pad24) -> VCC_SYSIN
- U4 pad 25: unconnected-(U4-SW3-Pad25) -> Net-(U4-SW3)
- U4 pad 26: unconnected-(U4-VBUCK3-Pad26) -> VCC_DDR
- U4 pad 27: unconnected-(U4-FB3-Pad27) -> Net-(U4-FB3)
- U4 pad 28: unconnected-(U4-LDO4-Pad28) -> VCCIO_ACODEC
- U4 pad 29: unconnected-(U4-LDO5-Pad29) -> VCCIO_SD
- U4 pad 3: unconnected-(U4-LDO7-Pad3) -> VCCA_1V8_P
- U4 pad 30: unconnected-(U4-VCC6-Pad30) -> VCC_SYSIN
- U4 pad 31: unconnected-(U4-LDO6-Pad31) -> VCC3V3_PMU
- U4 pad 32: unconnected-(U4-SPKP_OUT-Pad32) -> Net-(U4-SPKP_OUT)
- U4 pad 33: unconnected-(U4-VCC_SPK_HP-Pad33) -> Net-(U4-VCC_SPK_HP)
- U4 pad 34: unconnected-(U4-SPKN_OUT-Pad34) -> Net-(U4-SPKN_OUT)
- U4 pad 35: unconnected-(U4-VCC_CPVSS-Pad35) -> Net-(U4-VCC_CPVSS)
- U4 pad 36: unconnected-(U4-CPN-Pad36) -> Net-(U4-CPN)
- U4 pad 37: unconnected-(U4-CPP-Pad37) -> Net-(U4-CPP)
- U4 pad 38: unconnected-(U4-VCC_CPVDD-Pad38) -> Net-(U4-VCC_CPVDD)
- U4 pad 39: unconnected-(U4-HPL_OUT-Pad39) -> HPL_OUT
- U4 pad 4: unconnected-(U4-VCC7-Pad4) -> VCC_SYSIN
- U4 pad 40: unconnected-(U4-HP_SNS-Pad40) -> HP_SNS
- U4 pad 41: unconnected-(U4-HPR_OUT-Pad41) -> HPR_OUT
- U4 pad 42: unconnected-(U4-MICIN-Pad42) -> Net-(U4-MICIN)
- U4 pad 43: unconnected-(U4-MICIP-Pad43) -> Net-(U4-MICIP)
- U4 pad 44: unconnected-(U4-VCC_1P8A-Pad44) -> Net-(U4-VCC_1P8A)
- U4 pad 45: unconnected-(U4-VCC_RTC-Pad45) -> VCC_SYSIN
- U4 pad 46: unconnected-(U4-VREF-Pad46) -> Net-(U4-VREF)
- U4 pad 47: unconnected-(U4-GNDREF-Pad47) -> GND
- U4 pad 48: unconnected-(U4-VCC_1P8D-Pad48) -> Net-(U4-VCC_1P8D)
- U4 pad 49: unconnected-(U4-SLEEP-Pad49) -> PMIC_SLEEP_H
- U4 pad 5: unconnected-(U4-LDO8-Pad5) -> VCCA1V8_PMU
- U4 pad 50: unconnected-(U4-XIN-Pad50) -> /Power/PMIC_XIN
- U4 pad 51: unconnected-(U4-XOUT-Pad51) -> /Power/PMIC_XOUT
- U4 pad 52: unconnected-(U4-PWRON-Pad52) -> PMIC_PWRON
- U4 pad 53: unconnected-(U4-SW5-Pad53) -> Net-(U4-SW5)
- U4 pad 54: unconnected-(U4-VCC9-Pad54) -> VCC_SYSIN
- U4 pad 56: unconnected-(U4-BATDIV-Pad56) -> Net-(U4-BATDIV)
- U4 pad 57: unconnected-(U4-VCC8-Pad57) -> VCC3V3_SYS
- U4 pad 58: unconnected-(U4-SWOUT2-Pad58) -> VCC3V3_SD
- U4 pad 59: unconnected-(U4-FB5-Pad59) -> Net-(U4-FB5)
- U4 pad 6: unconnected-(U4-LDO9-Pad6) -> VCCA1V8_IMAGE_P
- U4 pad 61: unconnected-(U4-VDC-Pad61) -> Net-(U4-VDC)
- U4 pad 62: unconnected-(U4-SNSP-Pad62) -> /Power/SNSP
- U4 pad 63: unconnected-(U4-SNSN-Pad63) -> /Power/SNSN
- U4 pad 64: unconnected-(U4-FB4-Pad64) -> VDD_NPU
- U4 pad 65: unconnected-(U4-SW4-Pad65) -> Net-(U4-SW4)
- U4 pad 66: unconnected-(U4-VCC4-Pad66) -> VCC_SYSIN
- U4 pad 67: unconnected-(U4-RESETB-Pad67) -> RESETn
- U4 pad 68: unconnected-(U4-CLK32K-Pad68) -> Net-(U4-CLK32K)
- U4 pad 69: unconnected-(U4-EP-Pad69) -> GND
- U4 pad 7: unconnected-(U4-INT-Pad7) -> PMIC_INT_L
- U4 pad 8: unconnected-(U4-FB2-Pad8) -> VDD_GPU
- U4 pad 9: unconnected-(U4-SW2-Pad9) -> Net-(U4-SW2)

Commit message: change of camera
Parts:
- turned CN1 to 0 degrees
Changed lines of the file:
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@@
 	(footprint "lcsc:CONN-SMD_30P-P0.40_AXT530124"
 		(layer "F.Cu")
-		(at 225.1 54.775 -90)
+		(at 225.1 54.775)
 		(property "Reference" "CN1"
-			(at 0 -5.64 90)
+			(at 0 -5.64 0)
 			(layer "F.SilkS")
 			(effects
@@
 		)
 		(property "Value" "AXT530124_C2924271"
-			(at 0 5.64 90)
+			(at 0 5.64 0)
 			(layer "F.Fab")
 			(effects
@@
 		)
 		(property "Datasheet" ""
-			(at 0 0 90)
+			(at 0 0 0)
 			(layer "F.Fab")
 			(hide yes)
@@
 		)
 		(property "Description" ""
-			(at 0 0 90)
+			(at 0 0 0)
 			(layer "F.Fab")
 			(hide yes)
@@
 		)
 		(property "LCSC Part" "C2924271"
-			(at 0 0 270)
+			(at 0 0 0)
 			(unlocked yes)
 			(layer "F.Fab")
@@
 		(attr smd)
 		(fp_line
+			(start -4.25 -1.5)
+			(end -4.22 -1.5)
+			(stroke
+				(width 0.13)
+				(type solid)
+			)
+			(layer "F.SilkS")
+		)
+		(fp_line
 			(start -4.25 1.5)
 			(end -4.25 -1.5)
@@
 		)
 		(fp_line
+			(start 4.22 -1.5)
+			(end 4.25 -1.5)
+			(stroke
+				(width 0.13)
+				(type solid)
+			)
+			(layer "F.SilkS")
+		)
+		(fp_line
+			(start 4.25 -1.5)
+			(end 4.25 1.5)
+			(stroke
+				(width 0.13)
+				(type solid)
+			)
+			(layer "F.SilkS")
+		)
+		(fp_line
 			(start 4.25 1.5)
 			(end 4.22 1.5)
-			(stroke
-				(width 0.13)
-				(type solid)
-			)
-			(layer "F.SilkS")
-		)
-		(fp_line
-			(start -4.25 -1.5)
-			(end -4.22 -1.5)
-			(stroke
-				(width 0.13)
-				(type solid)
-			)
-			(layer "F.SilkS")
-		)
-		(fp_line
-			(start 4.22 -1.5)
-			(end 4.25 -1.5)
-			(stroke
-				(width 0.13)
-				(type solid)
-			)
-			(layer "F.SilkS")
-		)
-		(fp_line
-			(start 4.25 -1.5)
-			(end 4.25 1.5)
 			(stroke
 				(width 0.13)
@@
 		)
 		(fp_text user "${REFERENCE}"
-			(at 0 0 90)
+			(at 0 0 0)
 			(layer "F.Fab")
 			(effects
@@
 		)
 		(pad "1" smd rect
-			(at -2.8 1.64 270)
+			(at -2.8 1.64)
 			(size 0.2 1)
 			(layers "F.Cu" "F.Mask" "F.Paste")
@@
 		)
 		(pad "2" smd rect
-			(at -2.8 -1.64 270)
+			(at -2.8 -1.64)
 			(size 0.2 1)
 			(layers "F.Cu" "F.Mask" "F.Paste")
@@
 		)
 		(pad "3" smd rect
-			(at -2.4 1.64 270)
+			(at -2.4 1.64)
 			(size 0.2 1)
 			(layers "F.Cu" "F.Mask" "F.Paste")
@@
 		)
 		(pad "4" smd rect
-			(at -2.4 -1.64 270)
+			(at -2.4 -1.64)
 			(size 0.2 1)
 			(layers "F.Cu" "F.Mask" "F.Paste")
@@
 		)
 		(pad "5" smd rect
-			(at -2 1.64 270)
+			(at -2 1.64)
 			(size 0.2 1)
 			(layers "F.Cu" "F.Mask" "F.Paste")
@@
 		)
 		(pad "6" smd rect
-			(at -2 -1.64 270)
+			(at -2 -1.64)
 			(size 0.2 1)
 			(layers "F.Cu" "F.Mask" "F.Paste")
@@
 		)
 		(pad "7" smd rect
-			(at -1.6 1.64 270)
+			(at -1.6 1.64)
 			(size 0.2 1)
 			(layers "F.Cu" "F.Mask" "F.Paste")
@@
 		)
 		(pad "8" smd rect
-			(at -1.6 -1.64 270)
+			(at -1.6 -1.64)
 			(size 0.2 1)
 			(layers "F.Cu" "F.Mask" "F.Paste")
@@
 		)
 		(pad "9" smd rect
-			(at -1.2 1.64 270)
+			(at -1.2 1.64)
 			(size 0.2 1)
 			(layers "F.Cu" "F.Mask" "F.Paste")
@@
 		)
 		(pad "10" smd rect
-			(at -1.2 -1.64 270)
+			(at -1.2 -1.64)
 			(size 0.2 1)
 			(layers "F.Cu" "F.Mask" "F.Paste")
@@
 		)
 		(pad "11" smd rect
-			(at -0.8 1.64 270)
+			(at -0.8 1.64)
 			(size 0.2 1)
 			(layers "F.Cu" "F.Mask" "F.Paste")
@@
 		)
 		(pad "12" smd rect
-			(at -0.8 -1.64 270)
+			(at -0.8 -1.64)
 			(size 0.2 1)
 			(layers "F.Cu" "F.Mask" "F.Paste")
@@
 		)
 		(pad "13" smd rect
-			(at -0.4 1.64 270)
+			(at -0.4 1.64)
 			(size 0.2 1)
 			(layers "F.Cu" "F.Mask" "F.Paste")
@@
 		)
 		(pad "14" smd rect
-			(at -0.4 -1.64 270)
+			(at -0.4 -1.64)
 			(size 0.2 1)
 			(layers "F.Cu" "F.Mask" "F.Paste")
@@
 		)
 		(pad "15" smd rect
-			(at 0 1.64 270)
+			(at 0 1.64)
 			(size 0.2 1)
 			(layers "F.Cu" "F.Mask" "F.Paste")
@@
 		)
 		(pad "16" smd rect
-			(at 0 -1.64 270)
+			(at 0 -1.64)
 			(size 0.2 1)
 			(layers "F.Cu" "F.Mask" "F.Paste")
@@
 		)
 		(pad "17" smd rect
-			(at 0.4 1.64 270)
+			(at 0.4 1.64)
 			(size 0.2 1)
 			(layers "F.Cu" "F.Mask" "F.Paste")
@@
 		)
 		(pad "18" smd rect
-			(at 0.4 -1.64 270)
+			(at 0.4 -1.64)
 			(size 0.2 1)
 			(layers "F.Cu" "F.Mask" "F.Paste")
@@
 		)
 		(pad "19" smd rect
-			(at 0.8 1.64 270)
+			(at 0.8 1.64)
 			(size 0.2 1)
 			(layers "F.Cu" "F.Mask" "F.Paste")
@@
 		)
 		(pad "20" smd rect
-			(at 0.8 -1.64 270)
+			(at 0.8 -1.64)
 			(size 0.2 1)
 			(layers "F.Cu" "F.Mask" "F.Paste")
@@
 		)
 		(pad "21" smd rect
-			(at 1.2 1.64 270)
+			(at 1.2 1.64)
 			(size 0.2 1)
 			(layers "F.Cu" "F.Mask" "F.Paste")
@@
 		)
 		(pad "22" smd rect
-			(at 1.2 -1.64 270)
+			(at 1.2 -1.64)
 			(size 0.2 1)
 			(layers "F.Cu" "F.Mask" "F.Paste")
@@
 		)
 		(pad "23" smd rect
-			(at 1.6 1.64 270)
+			(at 1.6 1.64)
 			(size 0.2 1)
 			(layers "F.Cu" "F.Mask" "F.Paste")
@@
 		)
 		(pad "24" smd rect
-			(at 1.6 -1.64 270)
+			(at 1.6 -1.64)
 			(size 0.2 1)
 			(layers "F.Cu" "F.Mask" "F.Paste")
@@
 		)
 		(pad "25" smd rect
-			(at 2 1.64 270)
+			(at 2 1.64)
 			(size 0.2 1)
 			(layers "F.Cu" "F.Mask" "F.Paste")
@@
 		)
 		(pad "26" smd rect
-			(at 2 -1.64 270)
+			(at 2 -1.64)
 			(size 0.2 1)
 			(layers "F.Cu" "F.Mask" "F.Paste")
@@
 		)
 		(pad "27" smd rect
-			(at 2.4 1.64 270)
+			(at 2.4 1.64)
 			(size 0.2 1)
 			(layers "F.Cu" "F.Mask" "F.Paste")
@@
 		)
 		(pad "28" smd rect
-			(at 2.4 -1.64 270)
+			(at 2.4 -1.64)
 			(size 0.2 1)
 			(layers "F.Cu" "F.Mask" "F.Paste")
@@
 		)
 		(pad "29" smd rect
-			(at 2.8 1.64 270)
+			(at 2.8 1.64)
 			(size 0.2 1)
 			(layers "F.Cu" "F.Mask" "F.Paste")
@@
 		)
 		(pad "30" smd rect
-			(at 2.8 -1.64 270)
+			(at 2.8 -1.64)
 			(size 0.2 1)
 			(layers "F.Cu" "F.Mask" "F.Paste")
@@
 		)
 		(pad "MP1" smd rect
-			(at -3.7 -1.54 270)
+			(at -3.7 -1.54)
 			(size 0.7 1.2)
 			(layers "F.Cu" "F.Mask" "F.Paste")
@@
 		)
 		(pad "MP2" smd rect
-			(at -3.7 1.54 270)
+			(at -3.7 1.54)
 			(size 0.7 1.2)
 			(layers "F.Cu" "F.Mask" "F.Paste")
@@
 		)
 		(pad "MP3" smd rect
-			(at 3.7 1.54 270)
+			(at 3.7 1.54)
 			(size 0.7 1.2)
 			(layers "F.Cu" "F.Mask" "F.Paste")
 		)
 		(pad "MP4" smd rect
-			(at 3.7 -1.54 270)
+			(at 3.7 -1.54)
 			(size 0.7 1.2)
 			(layers "F.Cu" "F.Mask" "F.Paste")
